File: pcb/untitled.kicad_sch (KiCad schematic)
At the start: 48 parts, among them IC10 AD844_OPAMP_MEL, IC3 FOD814_OPTO_NOSHD, IC5 FOD814_OPTO_MEL, IC6 AD844_OPAMP_AL, IC7 FOD814_OPTO_AL, IC8 AD844_OPAMP_NOSHD, U2 REF192_NOSHD, U3 REF192_AL, U4 REF192_MEL

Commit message: Working Commit - Nov24
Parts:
- removed J_AD844: Conn_01x04, Connector_PinHeader_2.54mm:PinHeader_1x04_P2.54mm_Vertical, symbol Connector_Generic:Conn_01x04
- removed J_FOD814: Conn_01x06, Connector_PinHeader_2.54mm:PinHeader_1x06_P2.54mm_Vertical, symbol Connector_Generic:Conn_01x06
- removed J_REF192: Conn_01x03, Connector_PinHeader_2.54mm:PinHeader_1x03_P2.54mm_Vertical, symbol Connector_Generic:Conn_01x03
- added J4: Conn_01x02, Connector_PinHeader_2.54mm:PinHeader_1x02_P2.54mm_Vertical, symbol Connector_Generic:Conn_01x02
- added J_AD1, J_AD2, J_AD3: Conn_01x04, Connector_PinHeader_2.54mm:PinHeader_1x04_P2.54mm_Vertical, symbol Connector_Generic:Conn_01x04
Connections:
- net ADC1_IN10_OPTO_F_NOSHD: now also J_AD1.4 (Pin_4)
- net ADC1_IN11_OPTO_E_NOSHD: now also J_AD1.3 (Pin_3)
- net ADC1_IN12_OPTO_F_MEL: now also J_AD3.4 (Pin_4)
- net ADC1_IN13_OPTO_E_MEL: now also J_AD3.3 (Pin_3)
- net ADC1_IN14_OPTO_F_AL: now also J_AD2.4 (Pin_4)
- net ADC1_IN15_OPTO_E_AL: now also J_AD2.3 (Pin_3)
- net ADC1_IN1_OPAMP_NOSHD: now also J_AD1.1 (Pin_1)
- net ADC1_IN2_OPAMP_MEL: now also J_AD3.1 (Pin_1)
- net ADC1_IN3_OPAMP_AL: now also J_AD2.1 (Pin_1)
- net ADC1_IN4_VREF_NOSHD: now also J_AD1.2 (Pin_2)
- net ADC1_IN5_VREF_MEL: now also J_AD3.2 (Pin_2)
- net ADC1_IN6_VREF_AL: now also J_AD2.2 (Pin_2)
- net GND: now also J4.2 (Pin_2)
- net Signal Output: now also J4.1 (Pin_1)
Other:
- note added: "Signal Output Breakout"
- moved on the sheet: C22, C23, C28, C31, C32, C34, C37, C38, IC5, IC7, R19, R20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

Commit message: Added LM35 Temp Sensor
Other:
- note added: "Aluminum Shielded"
- note added: "Melanin Shielded"
- note added: "No Shield"
- moved on the sheet: C19, C20, C21, C22, C23, C24, C28, C29, C30, C31, C32, C34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

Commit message: Added missing decoupling capacitor + changed capacitors footprint
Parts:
- C22, C23, C24: footprint capstone:T495D -> Capacitor_SMD:C_0805_2012Metric
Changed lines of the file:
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@@
 			)
 		)
-		(property "Footprint" "capstone:T495D"
+		(property "Footprint" "Capacitor_SMD:C_0805_2012Metric"
 			(at 39.7 60.96 0)
 			(effects
@@
 			)
 		)
-		(property "Footprint" "capstone:T495D"
+		(property "Footprint" "Capacitor_SMD:C_0805_2012Metric"
 			(at 42.24 209.55 0)
 			(effects
@@
 			)
 		)
-		(property "Footprint" "capstone:T495D"
+		(property "Footprint" "Capacitor_SMD:C_0805_2012Metric"
 			(at 42.24 143.51 0)
 			(effects

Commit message: Added switchable inputs for opamps
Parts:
- removed J4: Conn_01x02, Connector_PinHeader_2.54mm:PinHeader_1x02_P2.54mm_Vertical, symbol Connector_Generic:Conn_01x02
- added JP1, JP2, JP3: SolderJumper_3_Open, Jumper:SolderJumper-3_P2.0mm_Open_TrianglePad1.0x1.5mm, symbol Jumper:SolderJumper_3_Open
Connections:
- net +5V: now also JP1.1 (A), JP2.1 (A), JP3.1 (A)
- net Signal Output: now also JP1.3 (B), JP2.3 (B), JP3.3 (B); no longer R15.2, R19.2, R23.2
- new net: JP3.2 (C), R23.2
- new net: JP1.2 (C), R15.2
- new net: JP2.2 (C), R19.2
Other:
- note removed: "Signal Output Breakout"

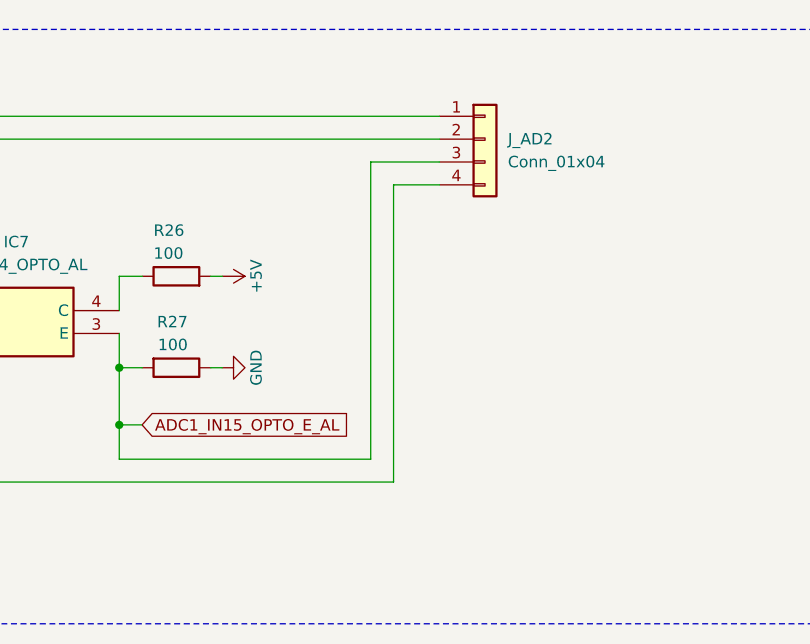
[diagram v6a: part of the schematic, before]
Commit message: Changed IC orientation
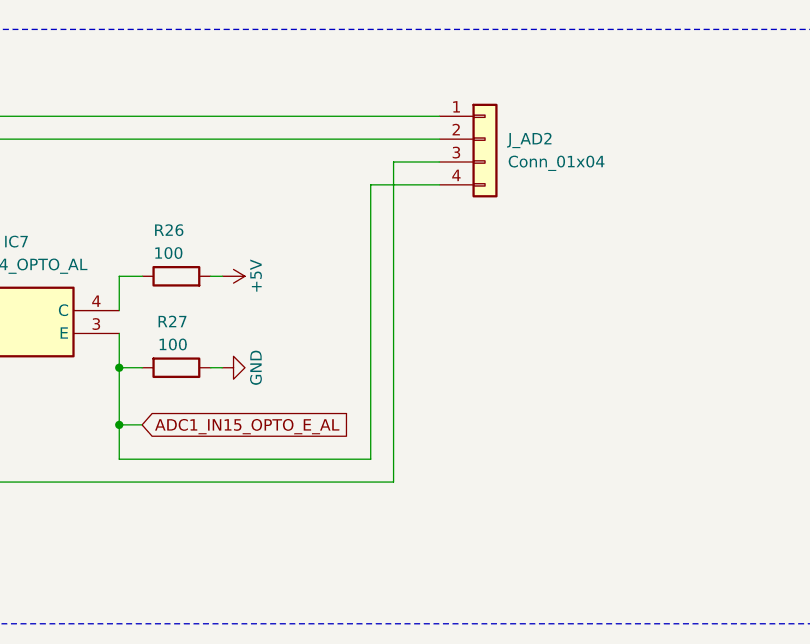
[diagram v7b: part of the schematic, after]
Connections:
- net ADC1_IN14_OPTO_F_AL: now also J_AD2.3 (Pin_3); no longer J_AD2.4 (Pin_4)
- net ADC1_IN15_OPTO_E_AL: now also J_AD2.4 (Pin_4); no longer J_AD2.3 (Pin_3)
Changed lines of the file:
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@@
+	(wire
+		(pts
+			(xy 317.5 144.78) (xy 317.5 114.3)
+		)
+		(stroke
+			(width 0)
+			(type default)
+		)
+	)
 	(wire
 		(pts
@@
 	(wire
 		(pts
+			(xy 317.5 114.3) (xy 325.12 114.3)
+		)
+		(stroke
+			(width 0)
+			(type default)
+		)
+	)
+	(wire
+		(pts
 			(xy 299.72 134.62) (xy 300.99 134.62)
 		)
@@
 	(wire
 		(pts
-			(xy 320.04 147.32) (xy 320.04 114.3)
-		)
-		(stroke
-			(width 0)
-			(type default)
-		)
-	)
-	(wire
-		(pts
 			(xy 288.29 189.23) (xy 290.83 189.23)
 		)
@@
 	(wire
 		(pts
-			(xy 317.5 144.78) (xy 317.5 111.76)
-		)
-		(stroke
-			(width 0)
-			(type default)
-		)
-	)
-	(wire
-		(pts
 			(xy 289.56 140.97) (xy 292.1 140.97)
 		)
@@
 	(wire
 		(pts
+			(xy 320.04 111.76) (xy 325.12 111.76)
+		)
+		(stroke
+			(width 0)
+			(type default)
+		)
+	)
+	(wire
+		(pts
 			(xy 288.29 195.58) (xy 288.29 199.39)
 		)
@@
 	(wire
 		(pts
+			(xy 320.04 111.76) (xy 320.04 147.32)
+		)
+		(stroke
+			(width 0)
+			(type default)
+		)
+	)
+	(wire
+		(pts
 			(xy 215.9 31.75) (xy 213.36 31.75)
 		)
@@
 	(wire
 		(pts
-			(xy 320.04 114.3) (xy 325.12 114.3)
-		)
-		(stroke
-			(width 0)
-			(type default)
-		)
-	)
-	(wire
-		(pts
 			(xy 138.43 213.36) (xy 138.43 219.71)
 		)
@@
 		)
 		(stroke
-			(width 0)
-			(type default)
-		)
-	)
-	(wire
-		(pts
-			(xy 317.5 111.76) (xy 325.12 111.76)
-		)
-		(stroke

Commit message: Changed C18, C19, C20, C28, C32, C34, C38, C41, C46, C47 footprints to 0805
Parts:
- C19, C20, C28, C32, C34, C38: footprint capstone:CAPC220145_88N_KEM-0.1u -> Capacitor_SMD:C_0805_2012Metric
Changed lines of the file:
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@@
 			)
 		)
-		(property "Footprint" "capstone:CAPC220145_88N_KEM-0.1u"
+		(property "Footprint" "Capacitor_SMD:C_0805_2012Metric"
 			(at 146.05 203.2 0)
 			(effects
@@
 			)
 		)
-		(property "Footprint" "capstone:CAPC220145_88N_KEM-0.1u"
+		(property "Footprint" "Capacitor_SMD:C_0805_2012Metric"
 			(at 143.51 54.61 0)
 			(effects
@@
 			)
 		)
-		(property "Footprint" "capstone:CAPC220145_88N_KEM-0.1u"
+		(property "Footprint" "Capacitor_SMD:C_0805_2012Metric"
 			(at 208.28 54.61 0)
 			(effects
@@
 			)
 		)
-		(property "Footprint" "capstone:CAPC220145_88N_KEM-0.1u"
+		(property "Footprint" "Capacitor_SMD:C_0805_2012Metric"
 			(at 210.82 203.2 0)
 			(effects
@@
 			)
 		)
-		(property "Footprint" "capstone:CAPC220145_88N_KEM-0.1u"
+		(property "Footprint" "Capacitor_SMD:C_0805_2012Metric"
 			(at 210.82 137.16 0)
 			(effects
@@
 			)
 		)
-		(property "Footprint" "capstone:CAPC220145_88N_KEM-0.1u"
+		(property "Footprint" "Capacitor_SMD:C_0805_2012Metric"
 			(at 146.05 137.16 0)
 			(effects
